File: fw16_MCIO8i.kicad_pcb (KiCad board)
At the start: 6 copper layers, 105.4 x 94.3 mm, 56 parts, among them U1 DS160PT801ACBR, U2 LMQ644A2QRXARQ1, U3 TPS62802YKAR

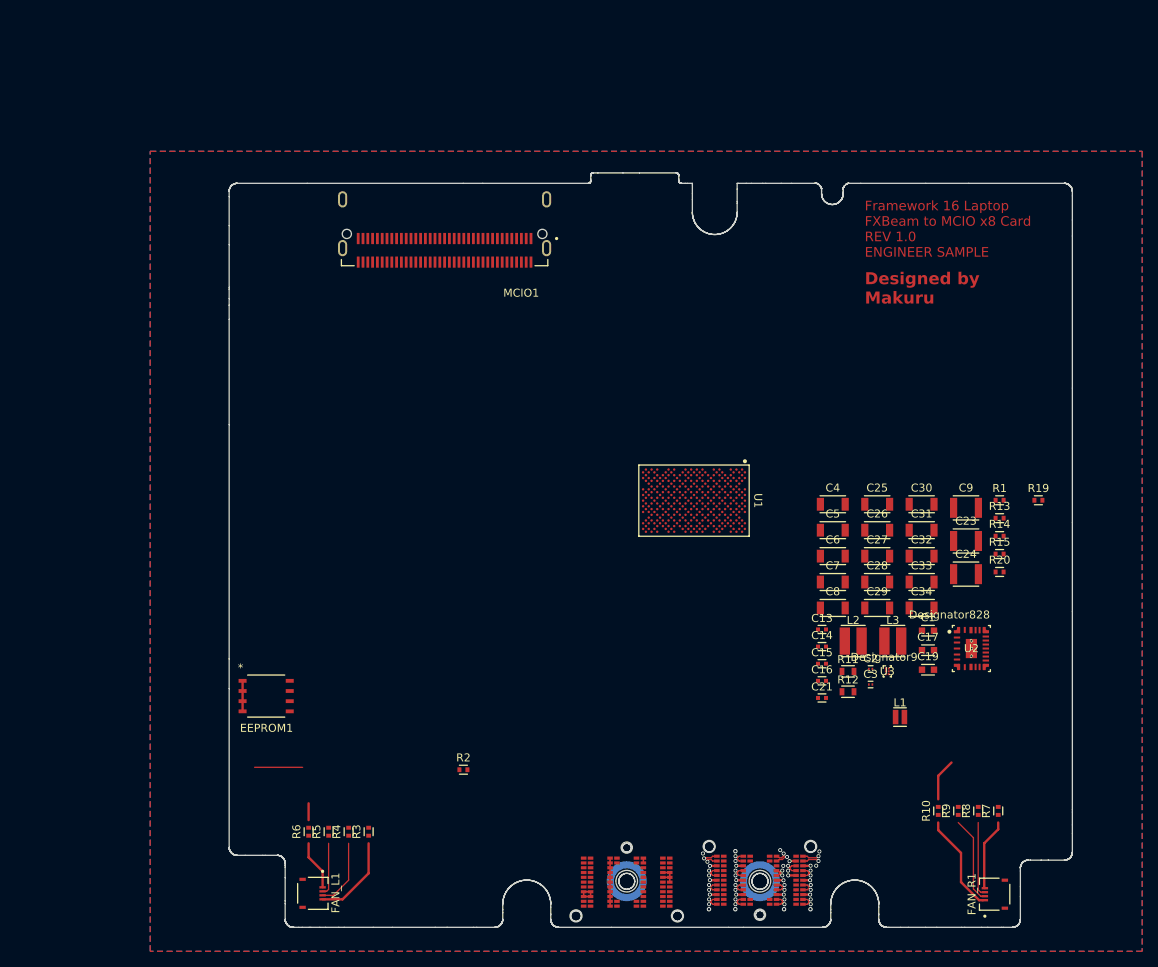
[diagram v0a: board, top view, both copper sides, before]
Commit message: Buck closer to recommended value
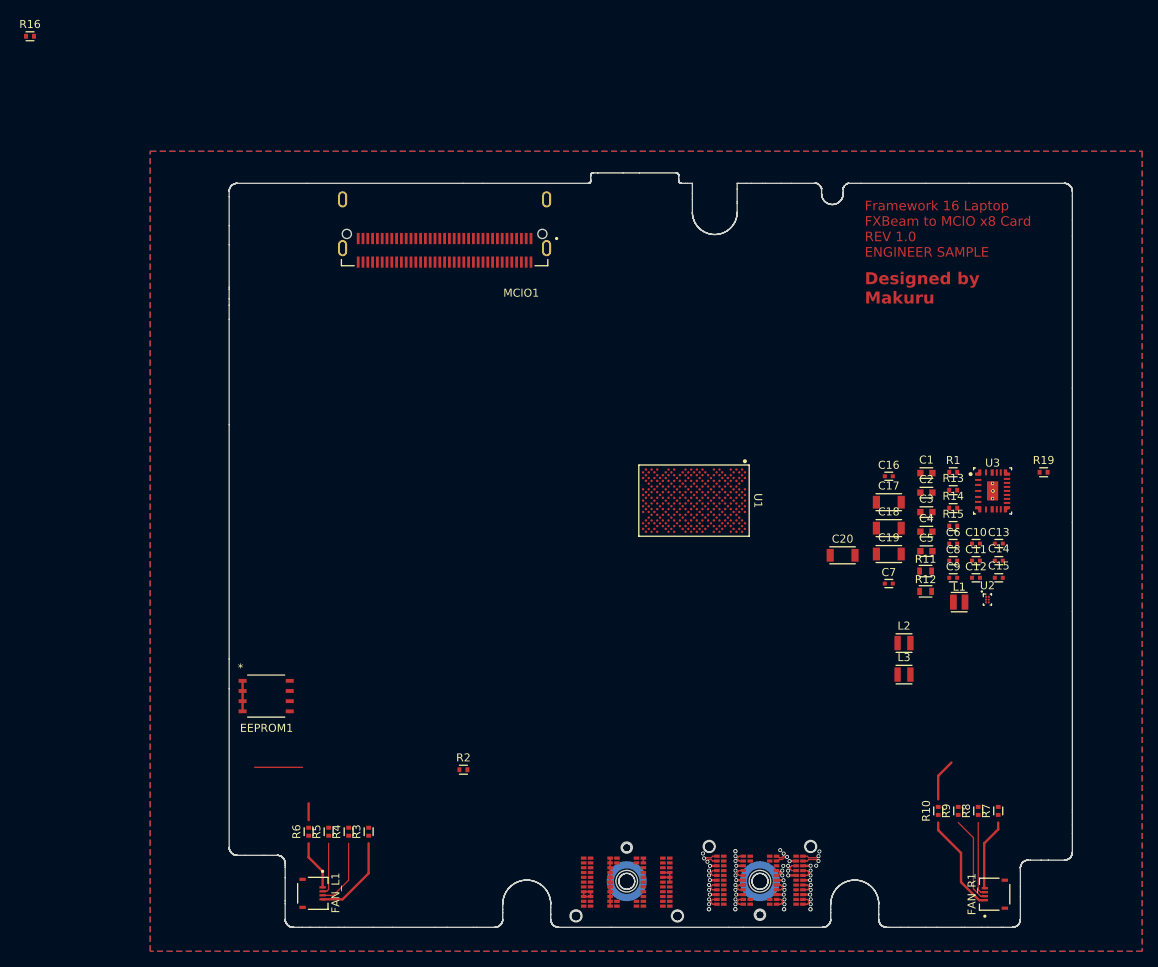
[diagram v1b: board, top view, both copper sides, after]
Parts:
- removed C21: 0402_885012205013, WE_WCAP-CSGP:C_Wurth_WCAP-CSGP-0402
- removed C23, C24: 1210_H2.0_885012209005, WE_WCAP-CSGP:C_Wurth_WCAP-CSGP-1210_H2.0
- removed C25, C26, C27, C28, C29, C30, C31, C32, C33, C34: 1206_H1.6_885012108012, WE_WCAP-CSGP:C_Wurth_WCAP-CSGP-1206_H1.6
- removed R20: 0402_560112110019, WE_WRIS-RSKS:R_Wurth_WRIS-RSKS-0402
- added C10: 0402_885012205018, WE_WCAP-CSGP:C_Wurth_WCAP-CSGP-0402, F.Cu at (119.2, 64.0)
- added C11: 0402_885012205018, WE_WCAP-CSGP:C_Wurth_WCAP-CSGP-0402, F.Cu at (119.2, 66.2)
- added C12: 0402_885012205017, WE_WCAP-CSGP:C_Wurth_WCAP-CSGP-0402, F.Cu at (119.2, 68.3)
- added C18: 1206_H1.6_885012208019, WE_WCAP-CSGP:C_Wurth_WCAP-CSGP-1206_H1.6, F.Cu at (108.3, 62.1)
- added C20: 1206_H1.6_885012208019, WE_WCAP-CSGP:C_Wurth_WCAP-CSGP-1206_H1.6, F.Cu at (102.5, 65.5)
- added R16: 0402_560112110215, WE_WRIS-RSKS:R_Wurth_WRIS-RSKS-0402, F.Cu at (0.93, 0.62)
- C1: value 0603_R_885012006001 -> 0603_Fl0.35_R_885012106031; footprint WE_WCAP-CSGP:C_Wurth_WCAP-CSGP-0603_R -> WE_WCAP-CSGP:C_Wurth_WCAP-CSGP-0603_Fl0.35_R
- C13: value 0402_885012205018 -> 0402_885012205013
- C14: value 0402_885012205018 -> 0402_885392005058; footprint WE_WCAP-CSGP:C_Wurth_WCAP-CSGP-0402 -> WE_WCAP-CSRF:C_Wurth_WCAP-CSRF-0402
- C15: value 0402_885012205017 -> 0402_885392005147; footprint WE_WCAP-CSGP:C_Wurth_WCAP-CSGP-0402 -> WE_WCAP-CSRF:C_Wurth_WCAP-CSRF-0402
- C16: value 0402_885012205013 -> 0402_885012105012
- C17: value 0603_R_885012006001 -> 1206_H1.6_885012208019; footprint WE_WCAP-CSGP:C_Wurth_WCAP-CSGP-0603_R -> WE_WCAP-CSGP:C_Wurth_WCAP-CSGP-1206_H1.6
- C19: value 0603_R_885012206021 -> 1206_H1.6_885012208019; footprint WE_WCAP-CSGP:C_Wurth_WCAP-CSGP-0603_R -> WE_WCAP-CSGP:C_Wurth_WCAP-CSGP-1206_H1.6
- C2, C3: value 0201_885012104002 -> 0603_Fl0.35_R_885012106031; footprint WE_WCAP-CSGP:C_Wurth_WCAP-CSGP-0201 -> WE_WCAP-CSGP:C_Wurth_WCAP-CSGP-0603_Fl0.35_R
- C4, C5: value 1206_H0.8_885012008001 -> 0603_Fl0.35_R_885012106031; footprint WE_WCAP-CSGP:C_Wurth_WCAP-CSGP-1206_H0.8 -> WE_WCAP-CSGP:C_Wurth_WCAP-CSGP-0603_Fl0.35_R
- C6, C8: value 1206_H0.8_885012008001 -> 0402_885012105022; footprint WE_WCAP-CSGP:C_Wurth_WCAP-CSGP-1206_H0.8 -> WE_WCAP-CSGP:C_Wurth_WCAP-CSGP-0402
- C7: value 1206_H0.8_885012008001 -> 0402_885012105012; footprint WE_WCAP-CSGP:C_Wurth_WCAP-CSGP-1206_H0.8 -> WE_WCAP-CSGP:C_Wurth_WCAP-CSGP-0402
- C9: value 1210_H1.25_885012209003 -> 0402_885012105022; footprint WE_WCAP-CSGP:C_Wurth_WCAP-CSGP-1210_H1.25 -> WE_WCAP-CSGP:C_Wurth_WCAP-CSGP-0402
- L1: value 1610_744383130082 -> 2010_744383430047; footprint WE-MAPI:L_Wurth_WE-MAPI-1610 -> WE-MAPI:L_Wurth_WE-MAPI-2010
- L2, L3: value 3012_744383340056 -> 201610_74479276124; footprint WE-MAPI:L_Wurth_WE-MAPI-3012 -> WE-PMCI:L_Wurth_WE-PMCI-201610
- R1: value 0402_560112110019 -> 0402_560112110020
- R13: value 0402_560112110020 -> 0402_560112110019
- R15: value 0402_560112110215 -> 0402_560112110019
- U2: value LMQ644A2QRXARQ1 -> TPS62802YKAR; footprint step-down-converter-1.17V:RXA0024A-MFG -> step-down-converter-1.8V:YKA0006ACAC
- U3: value TPS62802YKAR -> LMQ644A2QRXARQ1; footprint step-down-converter-1.8V:YKA0006ACAC -> step-down-converter-1.17V:RXA0024A-MFG
- moved C16 26.9 mm to (108.3, 55.6)
- moved U3 26.1 mm to (121.3, 57.5)
- moved C13 24.6 mm to (122.0, 64.0)
- moved C14 24.6 mm to (122.0, 66.2)
- moved C15 24.6 mm to (122.0, 68.3)
- moved C2 23.1 mm to (113.0, 57.7)
- moved C3 22.7 mm to (113.0, 60.1)
- moved C1 19.7 mm to (113.0, 55.2)
- moved C17 19.1 mm to (108.3, 58.9)
- moved C8 16.2 mm to (116.3, 66.2)
- moved L1 16.2 mm to (117.1, 71.3)
- moved R11 15.9 mm to (112.9, 67.5)
- moved R12 15.9 mm to (112.9, 70.0)
- moved C19 15.3 mm to (108.3, 65.3)
- moved C6 15.1 mm to (116.3, 64.0)
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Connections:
- C13 pad 1: Net-(U2-CB1) -> Net-(C13-Pad1)
- C13 pad 2: Net-(U2-SW1) -> GND
- C14 pad 1: Net-(U2-CB2) -> Net-(U3-VOSNS2_COMP)
- C14 pad 2: Net-(U2-SW2) -> GND
- C15 pad 1: Net-(U2-FB2_SS) -> /PCIe_retimer/PCIe_retimer_power/PWR.1_17V
- C15 pad 2: GND -> Net-(U3-FB1)
- C16 pad 1: Net-(C16-Pad1) -> /PCIe_retimer/PCIe_retimer_power/PWR.1_17V
- C17 pad 1: Net-(U2-VOSNS2_COMP) -> /PCIe_retimer/PCIe_retimer_power/PWR.1_17V
- C2 pad 2: Net-(C2-Pad2) -> GND
- C3 pad 2: Net-(C2-Pad2) -> GND
- C4 pad 2: Net-(C2-Pad2) -> GND
- C5 pad 2: Net-(C2-Pad2) -> GND
- C6 pad 2: Net-(C2-Pad2) -> GND
- C7 pad 1: /fxbeam/PWR.5V -> Net-(U3-VCC)
- C7 pad 2: Net-(C2-Pad2) -> GND
- C8 pad 1: GND -> /PCIe_retimer/PCIe_retimer_power/PWR.1_8V
- C8 pad 2: /PCIe_retimer/PCIe_retimer_power/PWR.1_8V -> GND
- C9 pad 1: Net-(U2-VCC) -> /PCIe_retimer/PCIe_retimer_power/PWR.1_8V
- L1 pad 1: Net-(U3-SW) -> Net-(U2-SW)
- L2 pad 1: Net-(U2-SW1) -> Net-(U3-SW1)
- L3 pad 1: Net-(U2-SW2) -> Net-(U3-SW2)
- R1 pad 1: Net-(U2-VCC) -> GND
- R1 pad 2: Net-(U2-PG1_MODE) -> GND
- R11 pad 1: GND -> Net-(U3-RT)
- R11 pad 2: Net-(U2-RT) -> GND
- R12 pad 1: GND -> Net-(U3-CONFIG)
- R12 pad 2: Net-(U2-CONFIG) -> GND
- R13 pad 1: GND -> Net-(U3-VCC)
- R13 pad 2: GND -> Net-(U3-PG1_MODE)
- R14 pad 1: Net-(U2-VOSNS2_COMP) -> Net-(U3-VOSNS2_COMP)
- R14 pad 2: Net-(C16-Pad1) -> Net-(C13-Pad1)
- R15 pad 1: Net-(U2-FB1) -> /PCIe_retimer/PCIe_retimer_power/PWR.1_17V
- R15 pad 2: GND -> Net-(U3-FB1)

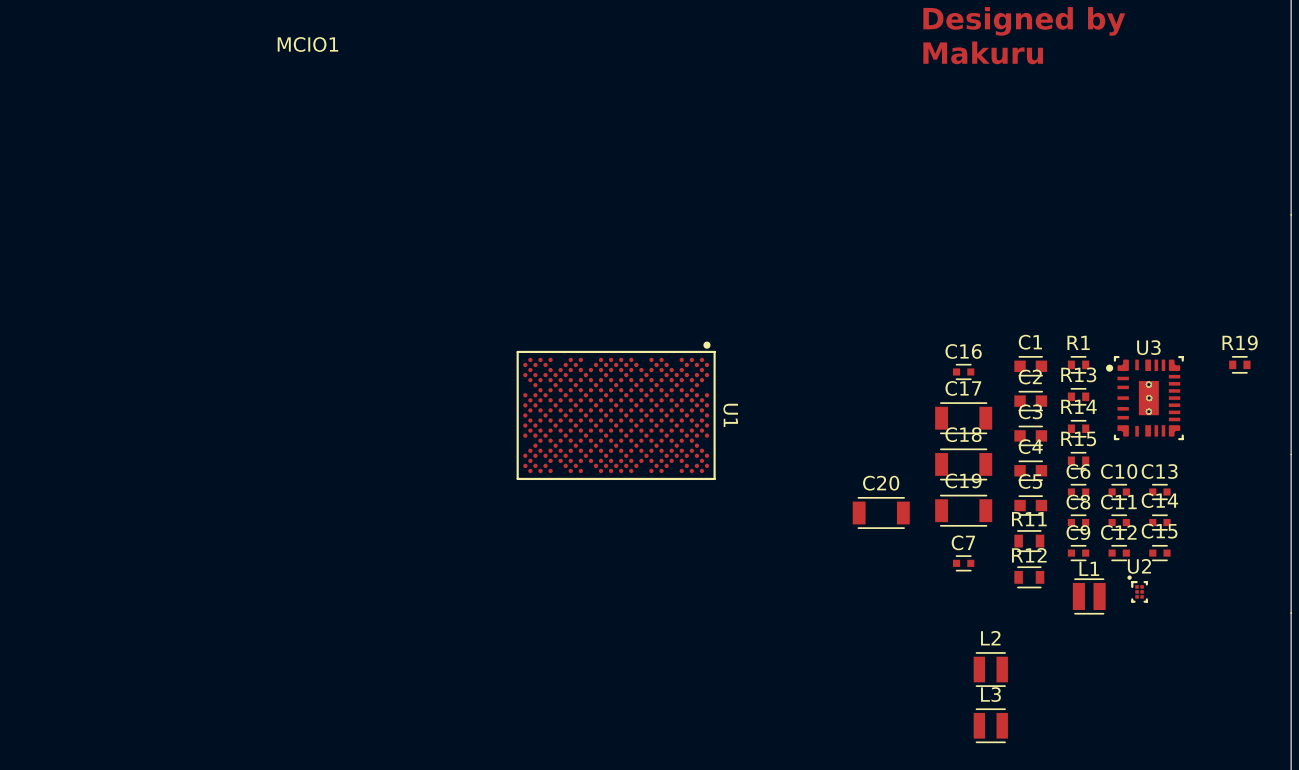
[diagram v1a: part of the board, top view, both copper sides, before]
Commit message: PCIe shematic fix
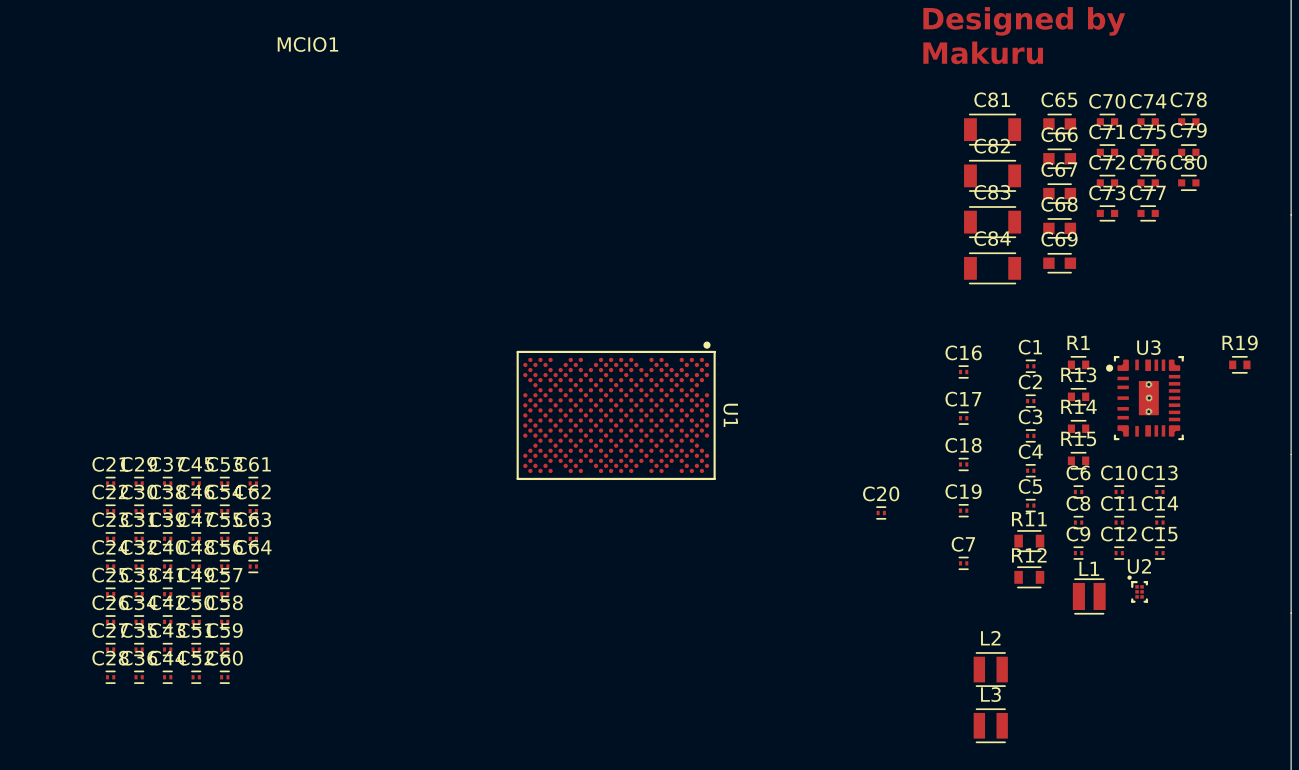
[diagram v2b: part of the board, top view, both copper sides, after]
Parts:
- added C21: 0201_885012104006, WE_WCAP-CSGP:C_Wurth_WCAP-CSGP-0201, F.Cu at (48.5, 63.4)
- added C22: 0201_885012104006, WE_WCAP-CSGP:C_Wurth_WCAP-CSGP-0201, F.Cu at (48.5, 65.4)
- added C23: 0201_885012104006, WE_WCAP-CSGP:C_Wurth_WCAP-CSGP-0201, F.Cu at (48.5, 67.3)
- added C24: 0201_885012104006, WE_WCAP-CSGP:C_Wurth_WCAP-CSGP-0201, F.Cu at (48.5, 69.2)
- added C25: 0201_885012104006, WE_WCAP-CSGP:C_Wurth_WCAP-CSGP-0201, F.Cu at (48.5, 71.2)
- added C26: 0201_885012104006, WE_WCAP-CSGP:C_Wurth_WCAP-CSGP-0201, F.Cu at (48.5, 73.1)
- added C27: 0201_885012104006, WE_WCAP-CSGP:C_Wurth_WCAP-CSGP-0201, F.Cu at (48.5, 75.1)
- added C28: 0201_885012104006, WE_WCAP-CSGP:C_Wurth_WCAP-CSGP-0201, F.Cu at (48.5, 77.0)
- added C29: 0201_885012104006, WE_WCAP-CSGP:C_Wurth_WCAP-CSGP-0201, F.Cu at (50.5, 63.4)
- added C30: 0201_885012104006, WE_WCAP-CSGP:C_Wurth_WCAP-CSGP-0201, F.Cu at (50.5, 65.4)
- added C31: 0201_885012104006, WE_WCAP-CSGP:C_Wurth_WCAP-CSGP-0201, F.Cu at (50.5, 67.3)
- added C32: 0201_885012104006, WE_WCAP-CSGP:C_Wurth_WCAP-CSGP-0201, F.Cu at (50.5, 69.2)
- added C33: 0201_885012104006, WE_WCAP-CSGP:C_Wurth_WCAP-CSGP-0201, F.Cu at (50.5, 71.2)
- added C34: 0201_885012104006, WE_WCAP-CSGP:C_Wurth_WCAP-CSGP-0201, F.Cu at (50.5, 73.1)
- added C35: 0201_885012104006, WE_WCAP-CSGP:C_Wurth_WCAP-CSGP-0201, F.Cu at (50.5, 75.1)
- added C36: 0201_885012104006, WE_WCAP-CSGP:C_Wurth_WCAP-CSGP-0201, F.Cu at (50.5, 77.0)
- added C37: 0201_885012104006, WE_WCAP-CSGP:C_Wurth_WCAP-CSGP-0201, F.Cu at (52.5, 63.4)
- added C38: 0201_885012104006, WE_WCAP-CSGP:C_Wurth_WCAP-CSGP-0201, F.Cu at (52.5, 65.4)
- added C39: 0201_885012104006, WE_WCAP-CSGP:C_Wurth_WCAP-CSGP-0201, F.Cu at (52.5, 67.3)
- added C40: 0201_885012104006, WE_WCAP-CSGP:C_Wurth_WCAP-CSGP-0201, F.Cu at (52.5, 69.2)
- added C41: 0201_885012104006, WE_WCAP-CSGP:C_Wurth_WCAP-CSGP-0201, F.Cu at (52.5, 71.2)
- added C42: 0201_885012104006, WE_WCAP-CSGP:C_Wurth_WCAP-CSGP-0201, F.Cu at (52.5, 73.1)
- added C43: 0201_885012104006, WE_WCAP-CSGP:C_Wurth_WCAP-CSGP-0201, F.Cu at (52.5, 75.1)
- added C44: 0201_885012104006, WE_WCAP-CSGP:C_Wurth_WCAP-CSGP-0201, F.Cu at (52.5, 77.0)
- added C45: 0201_885012104006, WE_WCAP-CSGP:C_Wurth_WCAP-CSGP-0201, F.Cu at (54.5, 63.4)
- added C46: 0201_885012104006, WE_WCAP-CSGP:C_Wurth_WCAP-CSGP-0201, F.Cu at (54.5, 65.4)
- added C47: 0201_885012104006, WE_WCAP-CSGP:C_Wurth_WCAP-CSGP-0201, F.Cu at (54.5, 67.3)
- added C48: 0201_885012104006, WE_WCAP-CSGP:C_Wurth_WCAP-CSGP-0201, F.Cu at (54.5, 69.2)
- added C49: 0201_885012104006, WE_WCAP-CSGP:C_Wurth_WCAP-CSGP-0201, F.Cu at (54.5, 71.2)
- added C50: 0201_885012104006, WE_WCAP-CSGP:C_Wurth_WCAP-CSGP-0201, F.Cu at (54.5, 73.1)
- added C51: 0201_885012104006, WE_WCAP-CSGP:C_Wurth_WCAP-CSGP-0201, F.Cu at (54.5, 75.1)
- added C52: 0201_885012104006, WE_WCAP-CSGP:C_Wurth_WCAP-CSGP-0201, F.Cu at (54.5, 77.0)
- added C53: 0201_885012104006, WE_WCAP-CSGP:C_Wurth_WCAP-CSGP-0201, F.Cu at (56.5, 63.4)
- added C54: 0201_885012104006, WE_WCAP-CSGP:C_Wurth_WCAP-CSGP-0201, F.Cu at (56.5, 65.4)
- added C55: 0201_885012104006, WE_WCAP-CSGP:C_Wurth_WCAP-CSGP-0201, F.Cu at (56.5, 67.3)
- added C56: 0201_885012104006, WE_WCAP-CSGP:C_Wurth_WCAP-CSGP-0201, F.Cu at (56.5, 69.2)
- added C57: 0201_885012104006, WE_WCAP-CSGP:C_Wurth_WCAP-CSGP-0201, F.Cu at (56.5, 71.2)
- added C58: 0201_885012104006, WE_WCAP-CSGP:C_Wurth_WCAP-CSGP-0201, F.Cu at (56.5, 73.1)
- added C59: 0201_885012104006, WE_WCAP-CSGP:C_Wurth_WCAP-CSGP-0201, F.Cu at (56.5, 75.1)
- added C60: 0201_885012104006, WE_WCAP-CSGP:C_Wurth_WCAP-CSGP-0201, F.Cu at (56.5, 77.0)
- added C61: 0201_885012104006, WE_WCAP-CSGP:C_Wurth_WCAP-CSGP-0201, F.Cu at (58.5, 63.4)
- added C62: 0201_885012104006, WE_WCAP-CSGP:C_Wurth_WCAP-CSGP-0201, F.Cu at (58.5, 65.4)
- added C63: 0201_885012104006, WE_WCAP-CSGP:C_Wurth_WCAP-CSGP-0201, F.Cu at (58.5, 67.3)
- added C64: 0201_885012104006, WE_WCAP-CSGP:C_Wurth_WCAP-CSGP-0201, F.Cu at (58.5, 69.2)
- added C65: 0603_Fl0.35_R_885012106031, WE_WCAP-CSGP:C_Wurth_WCAP-CSGP-0603_Fl0.35_R, F.Cu at (115.0, 38.2)
- added C66: 0603_Fl0.35_R_885012106031, WE_WCAP-CSGP:C_Wurth_WCAP-CSGP-0603_Fl0.35_R, F.Cu at (115.0, 40.7)
- added C67: 0603_Fl0.35_R_885012106031, WE_WCAP-CSGP:C_Wurth_WCAP-CSGP-0603_Fl0.35_R, F.Cu at (115.0, 43.1)
- added C68: 0603_Fl0.35_R_885012106031, WE_WCAP-CSGP:C_Wurth_WCAP-CSGP-0603_Fl0.35_R, F.Cu at (115.0, 45.6)
- added C69: 0603_Fl0.35_R_885012106031, WE_WCAP-CSGP:C_Wurth_WCAP-CSGP-0603_Fl0.35_R, F.Cu at (115.0, 48.0)
- added C70: 0402_885012105022, WE_WCAP-CSGP:C_Wurth_WCAP-CSGP-0402, F.Cu at (118.3, 38.1)
- added C71: 0402_885012105012, WE_WCAP-CSGP:C_Wurth_WCAP-CSGP-0402, F.Cu at (118.3, 40.2)
- added C72: 0402_885012105022, WE_WCAP-CSGP:C_Wurth_WCAP-CSGP-0402, F.Cu at (118.3, 42.4)
- added C73: 0402_885012105022, WE_WCAP-CSGP:C_Wurth_WCAP-CSGP-0402, F.Cu at (118.3, 44.5)
- added C74: 0402_885012205018, WE_WCAP-CSGP:C_Wurth_WCAP-CSGP-0402, F.Cu at (121.2, 38.1)
- added C75: 0402_885012205018, WE_WCAP-CSGP:C_Wurth_WCAP-CSGP-0402, F.Cu at (121.2, 40.2)
- added C76: 0402_885012205017, WE_WCAP-CSGP:C_Wurth_WCAP-CSGP-0402, F.Cu at (121.2, 42.4)
- added C77: 0402_885012205013, WE_WCAP-CSGP:C_Wurth_WCAP-CSGP-0402, F.Cu at (121.2, 44.5)
- added C78: 0402_885392005058, WE_WCAP-CSRF:C_Wurth_WCAP-CSRF-0402, F.Cu at (124.0, 38.1)
- added C79: 0402_885392005147, WE_WCAP-CSRF:C_Wurth_WCAP-CSRF-0402, F.Cu at (124.0, 40.2)
- added C80: 0402_885012105012, WE_WCAP-CSGP:C_Wurth_WCAP-CSGP-0402, F.Cu at (124.0, 42.4)
- added C81: 1206_H1.6_885012208019, WE_WCAP-CSGP:C_Wurth_WCAP-CSGP-1206_H1.6, F.Cu at (110.3, 38.6)
- added C82: 1206_H1.6_885012208019, WE_WCAP-CSGP:C_Wurth_WCAP-CSGP-1206_H1.6, F.Cu at (110.3, 41.9)
- added C83: 1206_H1.6_885012208019, WE_WCAP-CSGP:C_Wurth_WCAP-CSGP-1206_H1.6, F.Cu at (110.3, 45.1)
- added C84: 1206_H1.6_885012208019, WE_WCAP-CSGP:C_Wurth_WCAP-CSGP-1206_H1.6, F.Cu at (110.3, 48.4)
- C1, C2, C3, C4, C5: value 0603_Fl0.35_R_885012106031 -> 0201_885012104006; footprint WE_WCAP-CSGP:C_Wurth_WCAP-CSGP-0603_Fl0.35_R -> WE_WCAP-CSGP:C_Wurth_WCAP-CSGP-0201
- C10, C11: value 0402_885012205018 -> 0201_885012104006; footprint WE_WCAP-CSGP:C_Wurth_WCAP-CSGP-0402 -> WE_WCAP-CSGP:C_Wurth_WCAP-CSGP-0201
- C12: value 0402_885012205017 -> 0201_885012104006; footprint WE_WCAP-CSGP:C_Wurth_WCAP-CSGP-0402 -> WE_WCAP-CSGP:C_Wurth_WCAP-CSGP-0201
- C13: value 0402_885012205013 -> 0201_885012104006; footprint WE_WCAP-CSGP:C_Wurth_WCAP-CSGP-0402 -> WE_WCAP-CSGP:C_Wurth_WCAP-CSGP-0201
- C14: value 0402_885392005058 -> 0201_885012104006; footprint WE_WCAP-CSRF:C_Wurth_WCAP-CSRF-0402 -> WE_WCAP-CSGP:C_Wurth_WCAP-CSGP-0201
- C15: value 0402_885392005147 -> 0201_885012104006; footprint WE_WCAP-CSRF:C_Wurth_WCAP-CSRF-0402 -> WE_WCAP-CSGP:C_Wurth_WCAP-CSGP-0201
- C16, C7: value 0402_885012105012 -> 0201_885012104006; footprint WE_WCAP-CSGP:C_Wurth_WCAP-CSGP-0402 -> WE_WCAP-CSGP:C_Wurth_WCAP-CSGP-0201
- C17, C18, C19, C20: value 1206_H1.6_885012208019 -> 0201_885012104006; footprint WE_WCAP-CSGP:C_Wurth_WCAP-CSGP-1206_H1.6 -> WE_WCAP-CSGP:C_Wurth_WCAP-CSGP-0201
- C6, C8, C9: value 0402_885012105022 -> 0201_885012104006; footprint WE_WCAP-CSGP:C_Wurth_WCAP-CSGP-0402 -> WE_WCAP-CSGP:C_Wurth_WCAP-CSGP-0201
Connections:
- C1 pad 1: /fxbeam/PWR.5V -> /PCIe_retimer/A_TX.0-
- C1 pad 2: GND -> unconnected-(C1-Pad2)
- C10 pad 1: Net-(U3-CB1) -> /PCIe_retimer/A_TX.4+
- C10 pad 2: Net-(U3-SW1) -> unconnected-(C10-Pad2)
- C11 pad 1: Net-(U3-CB2) -> /PCIe_retimer/A_TX.5-
- C11 pad 2: Net-(U3-SW2) -> unconnected-(C11-Pad2)
- C12 pad 1: Net-(U3-FB2_SS) -> /PCIe_retimer/A_TX.5+
- C12 pad 2: GND -> unconnected-(C12-Pad2)
- C13 pad 1: Net-(C13-Pad1) -> /PCIe_retimer/A_TX.6-
- C13 pad 2: GND -> unconnected-(C13-Pad2)
- C14 pad 1: Net-(U3-VOSNS2_COMP) -> /PCIe_retimer/A_TX.6+
- C14 pad 2: GND -> unconnected-(C14-Pad2)
- C15 pad 1: /PCIe_retimer/PCIe_retimer_power/PWR.1_17V -> /PCIe_retimer/A_TX.7-
- C15 pad 2: Net-(U3-FB1) -> unconnected-(C15-Pad2)
- C16 pad 1: /PCIe_retimer/PCIe_retimer_power/PWR.1_17V -> /PCIe_retimer/A_TX.7+
- C16 pad 2: GND -> unconnected-(C16-Pad2)
- C17 pad 1: /PCIe_retimer/PCIe_retimer_power/PWR.1_17V -> /MCIO/B_TX.0-
- C17 pad 2: GND -> unconnected-(C17-Pad2)
- C18 pad 1: /PCIe_retimer/PCIe_retimer_power/PWR.1_17V -> /MCIO/B_TX.0+
- C18 pad 2: GND -> unconnected-(C18-Pad2)
- C19 pad 1: /PCIe_retimer/PCIe_retimer_power/PWR.1_17V -> /MCIO/B_TX.1-
- C19 pad 2: GND -> unconnected-(C19-Pad2)
- C2 pad 1: /fxbeam/PWR.5V -> /PCIe_retimer/A_TX.0+
- C2 pad 2: GND -> unconnected-(C2-Pad2)
- C20 pad 1: /PCIe_retimer/PCIe_retimer_power/PWR.1_17V -> /MCIO/B_TX.1+
- C20 pad 2: GND -> unconnected-(C20-Pad2)
- C3 pad 1: /fxbeam/PWR.5V -> /PCIe_retimer/A_TX.1-
- C3 pad 2: GND -> unconnected-(C3-Pad2)
- C4 pad 1: /fxbeam/PWR.5V -> /PCIe_retimer/A_TX.1+
- C4 pad 2: GND -> unconnected-(C4-Pad2)
- C5 pad 1: /fxbeam/PWR.5V -> /PCIe_retimer/A_TX.2-
- C5 pad 2: GND -> unconnected-(C5-Pad2)
- C6 pad 1: /fxbeam/PWR.5V -> /PCIe_retimer/A_TX.2+
- C6 pad 2: GND -> unconnected-(C6-Pad2)
- C7 pad 1: Net-(U3-VCC) -> /PCIe_retimer/A_TX.3-
- C7 pad 2: GND -> unconnected-(C7-Pad2)
- C8 pad 1: /PCIe_retimer/PCIe_retimer_power/PWR.1_8V -> /PCIe_retimer/A_TX.3+
- C8 pad 2: GND -> unconnected-(C8-Pad2)
- C9 pad 1: /PCIe_retimer/PCIe_retimer_power/PWR.1_8V -> /PCIe_retimer/A_TX.4-
- C9 pad 2: GND -> unconnected-(C9-Pad2)
- IN1 pad SA1: /PCIe_retimer/A_RX.6+ -> /PCIe_retimer/A_TX.6+
- IN1 pad SA3: /PCIe_retimer/A_RX.4+ -> /PCIe_retimer/A_TX.4+
- IN1 pad SA6: /PCIe_retimer/A_RX.3- -> /PCIe_retimer/A_TX.3-
- IN1 pad SA8: /PCIe_retimer/A_RX.1- -> /PCIe_retimer/A_TX.1-
- IN1 pad SB1: /PCIe_retimer/A_RX.6- -> /PCIe_retimer/A_TX.6-
- IN1 pad SB3: /PCIe_retimer/A_RX.4- -> /PCIe_retimer/A_TX.4-
- IN1 pad SB6: /PCIe_retimer/A_RX.3+ -> /PCIe_retimer/A_TX.3+
- IN1 pad SB8: /PCIe_retimer/A_RX.1+ -> /PCIe_retimer/A_TX.1+
- IN1 pad SD1: /PCIe_retimer/A_RX.7- -> /PCIe_retimer/A_TX.7-
- IN1 pad SD3: /PCIe_retimer/A_RX.5+ -> /PCIe_retimer/A_TX.5+
- IN1 pad SD6: /PCIe_retimer/A_RX.2- -> /PCIe_retimer/A_TX.2-
- IN1 pad SD8: /PCIe_retimer/A_RX.0- -> /PCIe_retimer/A_TX.0-
- IN1 pad SE1: /PCIe_retimer/A_RX.7+ -> /PCIe_retimer/A_TX.7+
- IN1 pad SE3: /PCIe_retimer/A_RX.5- -> /PCIe_retimer/A_TX.5-
- IN1 pad SE6: /PCIe_retimer/A_RX.2+ -> /PCIe_retimer/A_TX.2+
- IN1 pad SE8: /PCIe_retimer/A_RX.0+ -> /PCIe_retimer/A_TX.0+
- IN1 pad SG1: /PCIe_retimer/A_TX.7- -> /PCIe_retimer/A_RX.7-
- IN1 pad SG3: /PCIe_retimer/A_TX.5- -> /PCIe_retimer/A_RX.5-
- IN1 pad SG6: /PCIe_retimer/A_TX.2+ -> /PCIe_retimer/A_RX.2+
- IN1 pad SG8: /PCIe_retimer/A_TX.0- -> /PCIe_retimer/A_RX.0-
- IN1 pad SH1: /PCIe_retimer/A_TX.7+ -> /PCIe_retimer/A_RX.7+
- IN1 pad SH3: /PCIe_retimer/A_TX.5+ -> /PCIe_retimer/A_RX.5+
- IN1 pad SH6: /PCIe_retimer/A_TX.2- -> /PCIe_retimer/A_RX.2-
- IN1 pad SH8: /PCIe_retimer/A_TX.0+ -> /PCIe_retimer/A_RX.0+
- IN1 pad SK1: /PCIe_retimer/A_TX.6+ -> /PCIe_retimer/A_RX.6+
- IN1 pad SK3: /PCIe_retimer/A_TX.4+ -> /PCIe_retimer/A_RX.4+
- IN1 pad SK6: /PCIe_retimer/A_TX.3- -> /PCIe_retimer/A_RX.3-
- IN1 pad SK8: /PCIe_retimer/A_TX.1- -> /PCIe_retimer/A_RX.1-
- IN1 pad SL1: /PCIe_retimer/A_TX.6- -> /PCIe_retimer/A_RX.6-
- IN1 pad SL3: /PCIe_retimer/A_TX.4- -> /PCIe_retimer/A_RX.4-
- IN1 pad SL6: /PCIe_retimer/A_TX.3+ -> /PCIe_retimer/A_RX.3+
- IN1 pad SL8: /PCIe_retimer/A_TX.1+ -> /PCIe_retimer/A_RX.1+
- MCIO1 pad A14: /MCIO/B_RX.2+ -> /MCIO/B_TX.2+
- MCIO1 pad A15: /MCIO/B_RX.2- -> /MCIO/B_TX.2-
- MCIO1 pad A17: /MCIO/B_RX.3+ -> /MCIO/B_TX.3+
- MCIO1 pad A18: /MCIO/B_RX.3- -> /MCIO/B_TX.3-
- MCIO1 pad A2: /MCIO/B_RX.0+ -> /MCIO/B_TX.0+
- MCIO1 pad A20: /MCIO/B_RX.4+ -> /MCIO/B_TX.4+
- MCIO1 pad A21: /MCIO/B_RX.4- -> /MCIO/B_TX.4-
- MCIO1 pad A23: /MCIO/B_RX.5+ -> /MCIO/B_TX.5+
- MCIO1 pad A24: /MCIO/B_RX.5- -> /MCIO/B_TX.5-
- MCIO1 pad A3: /MCIO/B_RX.0- -> /MCIO/B_TX.0-
- MCIO1 pad A32: /MCIO/B_RX.6+ -> /MCIO/B_TX.6+
- MCIO1 pad A33: /MCIO/B_RX.6- -> /MCIO/B_TX.6-
- MCIO1 pad A35: /MCIO/B_RX.7+ -> /MCIO/B_TX.7+
- MCIO1 pad A36: /MCIO/B_RX.7- -> /MCIO/B_TX.7-
- MCIO1 pad A5: /MCIO/B_RX.1+ -> /MCIO/B_TX.1+
- MCIO1 pad A6: /MCIO/B_RX.1- -> /MCIO/B_TX.1-
- MCIO1 pad B14: unconnected-(MCIO1-PET2+-PadB14) -> /MCIO/B_RX.2+
- MCIO1 pad B15: unconnected-(MCIO1-PET2--PadB15) -> /MCIO/B_RX.2-
- MCIO1 pad B17: unconnected-(MCIO1-PET3+-PadB17) -> /MCIO/B_RX.3+
- MCIO1 pad B18: unconnected-(MCIO1-PET3--PadB18) -> /MCIO/B_RX.3-
- MCIO1 pad B2: unconnected-(MCIO1-PET0+-PadB2) -> /MCIO/B_RX.0+
- MCIO1 pad B20: unconnected-(MCIO1-PET4+-PadB20) -> /MCIO/B_RX.4+
- MCIO1 pad B21: unconnected-(MCIO1-PET4--PadB21) -> /MCIO/B_RX.4-
- MCIO1 pad B23: unconnected-(MCIO1-PET5+-PadB23) -> /MCIO/B_RX.5+
- MCIO1 pad B24: unconnected-(MCIO1-PET5--PadB24) -> /MCIO/B_RX.5-
- MCIO1 pad B3: unconnected-(MCIO1-PET0--PadB3) -> /MCIO/B_RX.0-
- MCIO1 pad B32: unconnected-(MCIO1-PET6+-PadB32) -> /MCIO/B_RX.6+
- MCIO1 pad B33: unconnected-(MCIO1-PET6--PadB33) -> /MCIO/B_RX.6-
- MCIO1 pad B35: unconnected-(MCIO1-PET7+-PadB35) -> /MCIO/B_RX.7+
- MCIO1 pad B36: unconnected-(MCIO1-PET7--PadB36) -> /MCIO/B_RX.7-
- MCIO1 pad B5: unconnected-(MCIO1-PET1+-PadB5) -> /MCIO/B_RX.1+
- MCIO1 pad B6: unconnected-(MCIO1-PET1--PadB6) -> /MCIO/B_RX.1-
- R14 pad 2: Net-(C13-Pad1) -> Net-(C77-Pad1)
- U1 pad A14: /PCIe_retimer/A_RX.0- -> /PCIe_retimer/A_RX.7+
- U1 pad A20: /PCIe_retimer/A_RX.2- -> /PCIe_retimer/A_RX.5+
- U1 pad AA22: /PCIe_retimer/A_RX.4- -> /PCIe_retimer/A_RX.3+
- U1 pad AB23: /PCIe_retimer/A_RX.4+ -> /PCIe_retimer/A_RX.3-
- U1 pad AD21: /PCIe_retimer/A_RX.5- -> /PCIe_retimer/A_RX.2+
- U1 pad AE20: /PCIe_retimer/A_RX.5+ -> /PCIe_retimer/A_RX.2-
- U1 pad AG22: /PCIe_retimer/A_RX.6- -> /PCIe_retimer/A_RX.1+
- U1 pad AH23: /PCIe_retimer/A_RX.6+ -> /PCIe_retimer/A_RX.1-
- U1 pad AK21: /PCIe_retimer/A_RX.7- -> /PCIe_retimer/A_RX.0+
- U1 pad AL20: /PCIe_retimer/A_RX.7+ -> /PCIe_retimer/A_RX.0-
- U1 pad AN2: /PCIe_retimer/B_TX.4- -> /MCIO/B_RX.4-
- U1 pad AN22: /PCIe_retimer/B_RX.4- -> /MCIO/B_TX.4-
- U1 pad AP1: /PCIe_retimer/B_TX.4+ -> /MCIO/B_RX.4+
- U1 pad AP17: /PCIe_retimer/B_RX.6+ -> /MCIO/B_TX.6+
- U1 pad AP23: /PCIe_retimer/B_RX.4+ -> /MCIO/B_TX.4+
- U1 pad AP7: /PCIe_retimer/B_TX.6+ -> /MCIO/B_RX.6+
- U1 pad AR18: /PCIe_retimer/B_RX.6- -> /MCIO/B_TX.6-
- U1 pad AR6: /PCIe_retimer/B_TX.6- -> /MCIO/B_RX.6-
- U1 pad AT15: /PCIe_retimer/B_RX.7- -> /MCIO/B_TX.7-
- U1 pad AT21: /PCIe_retimer/B_RX.5- -> /MCIO/B_TX.5-
- U1 pad AT3: /PCIe_retimer/B_TX.5- -> /MCIO/B_RX.5-
- U1 pad AT9: /PCIe_retimer/B_TX.7- -> /MCIO/B_RX.7-
- U1 pad AU10: /PCIe_retimer/B_TX.7+ -> /MCIO/B_RX.7+
- U1 pad AU14: /PCIe_retimer/B_RX.7+ -> /MCIO/B_TX.7+
- U1 pad AU20: /PCIe_retimer/B_RX.5+ -> /MCIO/B_TX.5+
- U1 pad AU4: /PCIe_retimer/B_TX.5+ -> /MCIO/B_RX.5+
- U1 pad B15: /PCIe_retimer/A_RX.0+ -> /PCIe_retimer/A_RX.7-
- U1 pad B21: /PCIe_retimer/A_RX.2+ -> /PCIe_retimer/A_RX.5-
- U1 pad C18: /PCIe_retimer/A_RX.1+ -> /PCIe_retimer/A_RX.6-
- U1 pad D17: /PCIe_retimer/A_RX.1- -> /PCIe_retimer/A_RX.6+
- U1 pad D23: /PCIe_retimer/A_RX.3- -> /PCIe_retimer/A_RX.4+
- U1 pad E22: /PCIe_retimer/A_RX.3+ -> /PCIe_retimer/A_RX.4-
- U1 pad G20: /PCIe_retimer/B_RX.0- -> /MCIO/B_TX.0-
- U1 pad G4: /PCIe_retimer/B_TX.0- -> /MCIO/B_RX.0-
- U1 pad H21: /PCIe_retimer/B_RX.0+ -> /MCIO/B_TX.0+
- U1 pad H3: /PCIe_retimer/B_TX.0+ -> /MCIO/B_RX.0+
- U1 pad K1: /PCIe_retimer/B_TX.1- -> /MCIO/B_RX.1-
- U1 pad K23: /PCIe_retimer/B_RX.1- -> /MCIO/B_TX.1-
- U1 pad L2: /PCIe_retimer/B_TX.1+ -> /MCIO/B_RX.1+
- U1 pad L22: /PCIe_retimer/B_RX.1+ -> /MCIO/B_TX.1+
- U1 pad N20: /PCIe_retimer/B_RX.2- -> /MCIO/B_TX.2-
- U1 pad N4: /PCIe_retimer/B_TX.2- -> /MCIO/B_RX.2-
- U1 pad P21: /PCIe_retimer/B_RX.2+ -> /MCIO/B_TX.2+
- U1 pad P3: /PCIe_retimer/B_TX.2+ -> /MCIO/B_RX.2+
- U1 pad T1: /PCIe_retimer/B_TX.3- -> /MCIO/B_RX.3-
- U1 pad T23: /PCIe_retimer/B_RX.3- -> /MCIO/B_TX.3-
- U1 pad U2: /PCIe_retimer/B_TX.3+ -> /MCIO/B_RX.3+
- U1 pad U22: /PCIe_retimer/B_RX.3+ -> /MCIO/B_TX.3+
- U1 pad V19: /PCIe_retimer/PEXOUT.CLK- -> /MCIO/PEXOUT.CLK-
- U1 pad Y19: /PCIe_retimer/PEXOUT.CLK+ -> /MCIO/PEXOUT.CLK+
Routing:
- net /PCIe_retimer/A_TX.5+: track 41.6 -> 11.3 mm
- net /PCIe_retimer/A_RX.5+: track 11.3 -> 41.6 mm
- net /PCIe_retimer/A_TX.5-: track 41.0 -> 12.0 mm
- net /PCIe_retimer/A_RX.5-: track 12.0 -> 41.0 mm
- net /PCIe_retimer/A_TX.1-: track 24.7 -> 15.9 mm
- net /PCIe_retimer/A_RX.1-: track 15.9 -> 24.7 mm
- net /PCIe_retimer/A_TX.1+: track 25.3 -> 16.6 mm
- net /PCIe_retimer/A_RX.1+: track 16.6 -> 25.3 mm
- net /PCIe_retimer/A_TX.0+: track 24.1 -> 18.2 mm
- net /PCIe_retimer/A_RX.0+: track 18.2 -> 24.1 mm
- net /PCIe_retimer/A_TX.0-: track 23.5 -> 17.7 mm
- net /PCIe_retimer/A_RX.0-: track 17.7 -> 23.5 mm
- net /PCIe_retimer/A_TX.6-: track 7.89 -> 2.10 mm
- net /PCIe_retimer/A_RX.6-: track 2.10 -> 7.89 mm
- net /PCIe_retimer/A_TX.6+: track 7.71 -> 2.10 mm
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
